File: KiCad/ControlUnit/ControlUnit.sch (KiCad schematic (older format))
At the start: 0 parts

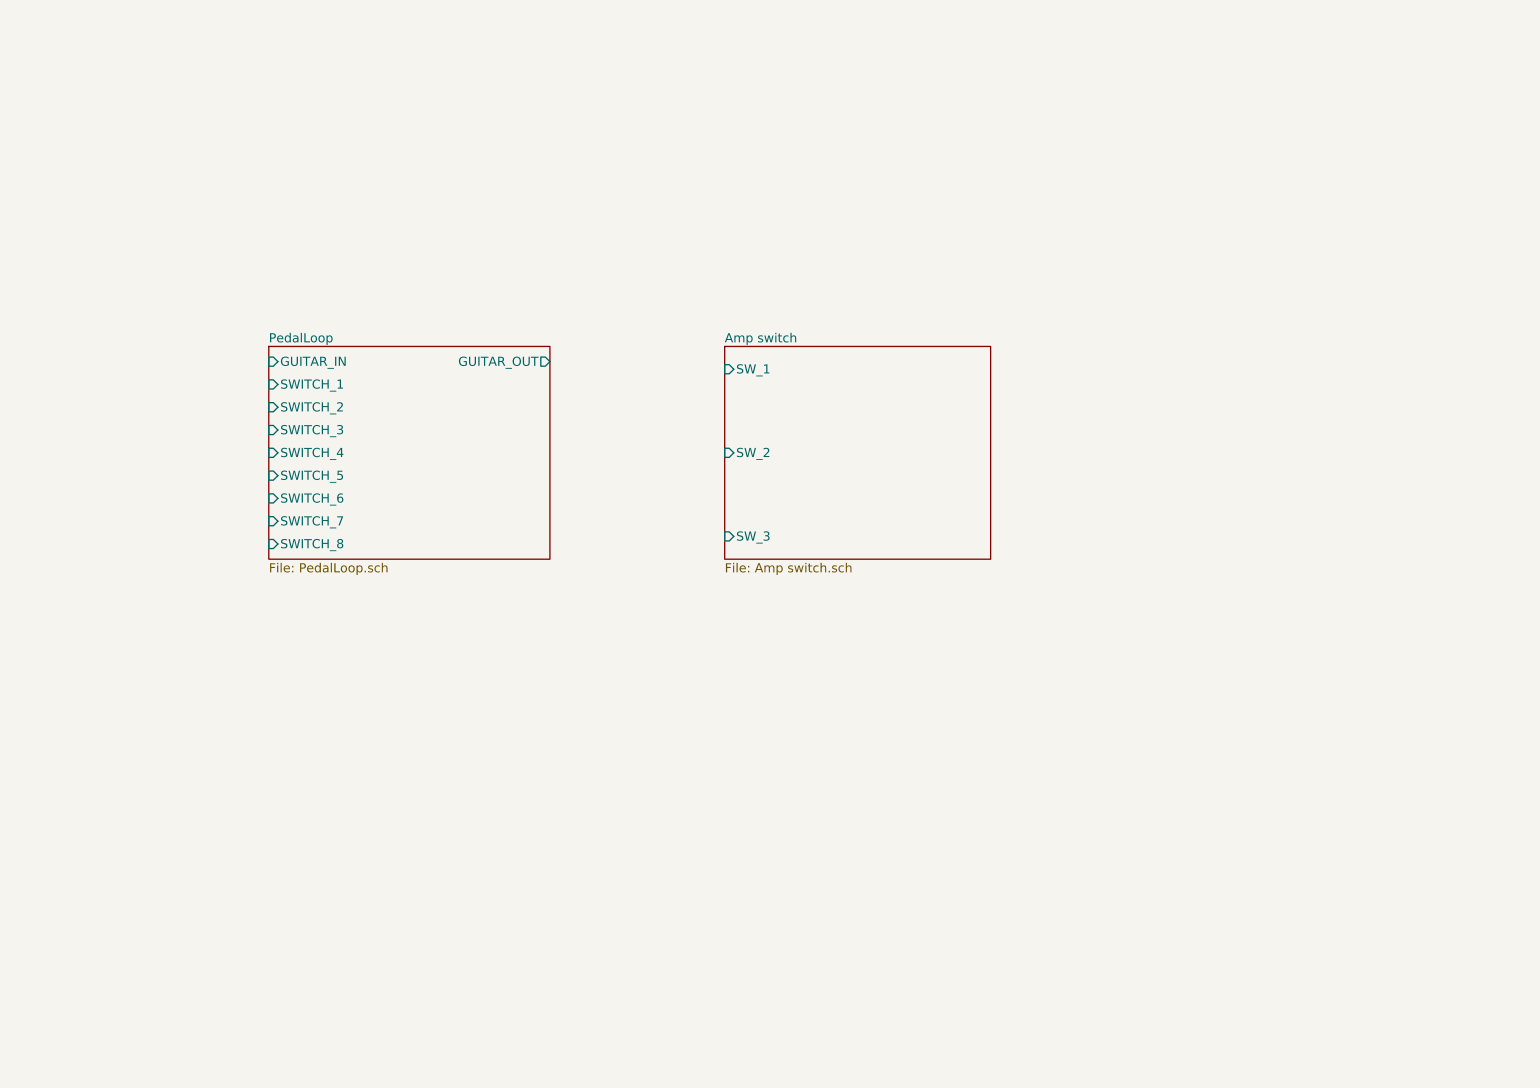
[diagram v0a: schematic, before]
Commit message: Added software for the prototype and made a netlist with footprints for the control unit board
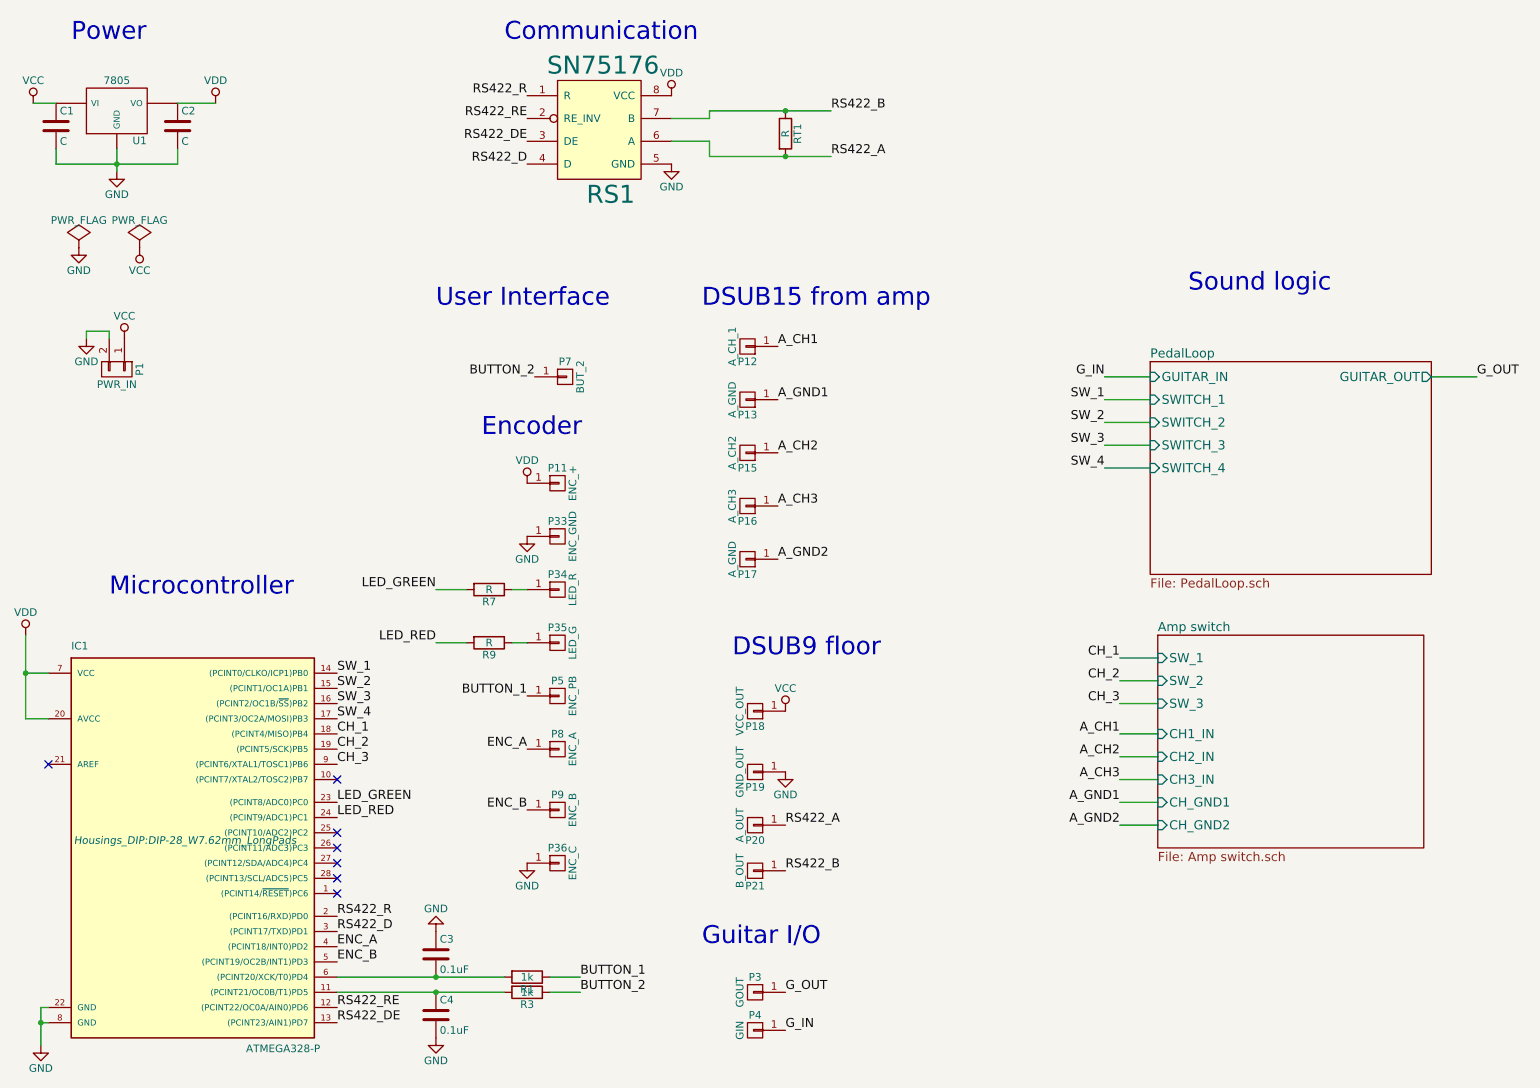
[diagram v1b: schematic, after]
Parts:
- added C1, C2: C, Capacitors_ThroughHole:C_Radial_D8_L13_P3.8, symbol C
- added C3, C4: 0.1uF, Capacitors_ThroughHole:C_Radial_D8_L13_P3.8, symbol C
- added IC1: ATMEGA328-P, Housings_DIP:DIP-28_W7.62mm_LongPads, symbol ATMEGA328-P
- added P1: PWR_IN, Socket_Strips:Socket_Strip_Straight_1x02, symbol CONN_01X02
- added P11: ENC_+, Pin_Headers:Pin_Header_Straight_1x01, symbol CONN_01X01
- added P12: A_CH_1, Pin_Headers:Pin_Header_Straight_1x01, symbol CONN_01X01
- added P13, P17: A_GND, Pin_Headers:Pin_Header_Straight_1x01, symbol CONN_01X01
- added P15: A_CH2, Pin_Headers:Pin_Header_Straight_1x01, symbol CONN_01X01
- added P16: A_CH3, Pin_Headers:Pin_Header_Straight_1x01, symbol CONN_01X01
- added P18: VCC_OUT, Pin_Headers:Pin_Header_Straight_1x01, symbol CONN_01X01
- added P19: GND_OUT, Pin_Headers:Pin_Header_Straight_1x01, symbol CONN_01X01
- added P20: A_OUT, Pin_Headers:Pin_Header_Straight_1x01, symbol CONN_01X01
- added P21: B_OUT, Pin_Headers:Pin_Header_Straight_1x01, symbol CONN_01X01
- added P3: GOUT, Pin_Headers:Pin_Header_Straight_1x01, symbol CONN_01X01
- added P33: ENC_GND, Pin_Headers:Pin_Header_Straight_1x01, symbol CONN_01X01
- added P34: LED_R, Pin_Headers:Pin_Header_Straight_1x01, symbol CONN_01X01
- added P35: LED_G, Pin_Headers:Pin_Header_Straight_1x01, symbol CONN_01X01
- added P36: ENC_C, Pin_Headers:Pin_Header_Straight_1x01, symbol CONN_01X01
- added P4: GIN, Pin_Headers:Pin_Header_Straight_1x01, symbol CONN_01X01
- added P5: ENC_PB, Pin_Headers:Pin_Header_Straight_1x01, symbol CONN_01X01
- added P7: BUT_2, Pin_Headers:Pin_Header_Straight_1x01, symbol CONN_01X01
- added P8: ENC_A, Pin_Headers:Pin_Header_Straight_1x01, symbol CONN_01X01
- added P9: ENC_B, Pin_Headers:Pin_Header_Straight_1x01, symbol CONN_01X01
- added R1, R3: 1k, Resistors_ThroughHole:Resistor_Vertical_RM5mm, symbol R
- added R7, R9, RT1: R, Resistors_ThroughHole:Resistor_Vertical_RM5mm, symbol R
- added RS1: SN75176, Housings_DIP:DIP-8_W7.62mm_LongPads, symbol SN75176
- added U1: 7805, TO_SOT_Packages_THT:SOT126_SOT32_Housing_Vertical_BigPads, symbol 7805
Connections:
- new net: C4.1, IC1.11 ((PCINT21/OC0B/T1)PD5), R3.2
- new net: C3.2, IC1.6 ((PCINT20/XCK/T0)PD4), R1.2
- new net: P35.1 (P1), R9.1
- new net: P34.1 (P1), R7.1
- new net A_CH1: P12.1 (P1)
- new net A_CH2: P15.1 (P1)
- new net A_CH3: P16.1 (P1)
- new net A_GND1: P13.1 (P1)
- new net A_GND2: P17.1 (P1)
- new net BUTTON_1: P5.1 (P1), R1.1
- new net BUTTON_2: P7.1 (P1), R3.1
- new net CH_1: IC1.18 ((PCINT4/MISO)PB4)
- new net CH_2: IC1.19 ((PCINT5/SCK)PB5)
- new net CH_3: IC1.9 ((PCINT6/XTAL1/TOSC1)PB6)
- new net ENC_A: IC1.4 ((PCINT18/INT0)PD2), P8.1 (P1)
- new net ENC_B: IC1.5 ((PCINT19/OC2B/INT1)PD3), P9.1 (P1)
- new net GND: C1.2, C2.2, C3.1, C4.2, IC1.22 (GND), IC1.8 (GND), P1.2 (P2), P19.1 (P1), P33.1 (P1), P36.1 (P1), RS1.5 (GND), U1.GND
- new net G_IN: P4.1 (P1)
- new net G_OUT: P3.1 (P1)
- new net LED_GREEN: IC1.23 ((PCINT8/ADC0)PC0), R7.2
- new net LED_RED: IC1.24 ((PCINT9/ADC1)PC1), R9.2
- new net RS422_A: P20.1 (P1), RS1.6 (A), RT1.2
- new net RS422_B: P21.1 (P1), RS1.7 (B), RT1.1
- new net RS422_D: IC1.3 ((PCINT17/TXD)PD1), RS1.4 (D)
- new net RS422_DE: IC1.13 ((PCINT23/AIN1)PD7), RS1.3 (DE)
- new net RS422_R: IC1.2 ((PCINT16/RXD)PD0), RS1.1 (R)
- new net RS422_RE: IC1.12 ((PCINT22/OC0A/AIN0)PD6), RS1.2 (RE_INV)
- new net SW_1: IC1.14 ((PCINT0/CLKO/ICP1)PB0)
- new net SW_2: IC1.15 ((PCINT1/OC1A)PB1)
- new net SW_3: IC1.16 ((PCINT2/OC1B/~SS~)PB2)
- new net SW_4: IC1.17 ((PCINT3/OC2A/MOSI)PB3)
- new net VCC: C1.1, P1.1 (P1), P18.1 (P1), U1.VI
- new net VDD: C2.1, IC1.20 (AVCC), IC1.7 (VCC), P11.1 (P1), RS1.8 (VCC), U1.VO
- no-connect marks 0 -> 7
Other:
- note added: "Communication"
- note added: "DSUB15 from amp"
- note added: "DSUB9 floor"
- note added: "Encoder"
- note added: "Guitar I/O"
- note added: "Microcontroller"
- note added: "Power"
- note added: "Sound logic"
- note added: "User Interface"

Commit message: Fine tuned PCB design and added multicontact connectors instead of  single connectors
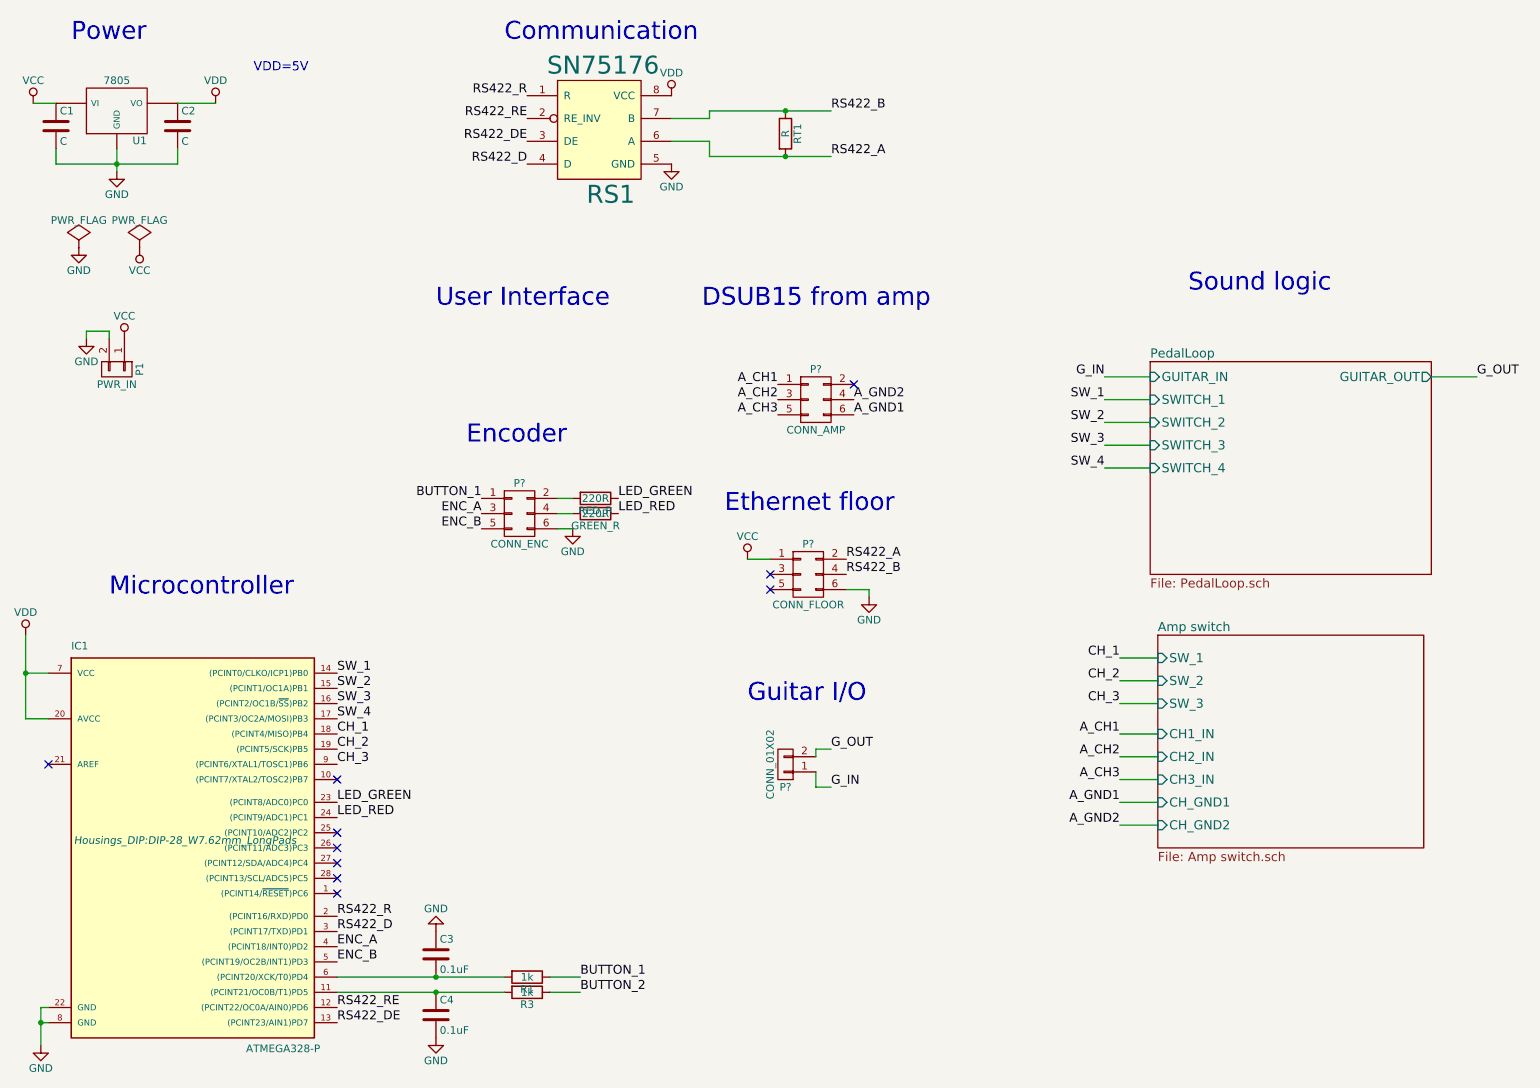
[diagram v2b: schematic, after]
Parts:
- removed P11: ENC_+, Pin_Headers:Pin_Header_Straight_1x01, symbol CONN_01X01
- removed P12: A_CH_1, Pin_Headers:Pin_Header_Straight_1x01, symbol CONN_01X01
- removed P13, P17: A_GND, Pin_Headers:Pin_Header_Straight_1x01, symbol CONN_01X01
- removed P15: A_CH2, Pin_Headers:Pin_Header_Straight_1x01, symbol CONN_01X01
- removed P16: A_CH3, Pin_Headers:Pin_Header_Straight_1x01, symbol CONN_01X01
- removed P18: VCC_OUT, Pin_Headers:Pin_Header_Straight_1x01, symbol CONN_01X01
- removed P19: GND_OUT, Pin_Headers:Pin_Header_Straight_1x01, symbol CONN_01X01
- removed P20: A_OUT, Pin_Headers:Pin_Header_Straight_1x01, symbol CONN_01X01
- removed P21: B_OUT, Pin_Headers:Pin_Header_Straight_1x01, symbol CONN_01X01
- removed P3: GOUT, Pin_Headers:Pin_Header_Straight_1x01, symbol CONN_01X01
- removed P33: ENC_GND, Pin_Headers:Pin_Header_Straight_1x01, symbol CONN_01X01
- removed P34: LED_R, Pin_Headers:Pin_Header_Straight_1x01, symbol CONN_01X01
- removed P35: LED_G, Pin_Headers:Pin_Header_Straight_1x01, symbol CONN_01X01
- removed P36: ENC_C, Pin_Headers:Pin_Header_Straight_1x01, symbol CONN_01X01
- removed P4: GIN, Pin_Headers:Pin_Header_Straight_1x01, symbol CONN_01X01
- removed P5: ENC_PB, Pin_Headers:Pin_Header_Straight_1x01, symbol CONN_01X01
- removed P7: BUT_2, Pin_Headers:Pin_Header_Straight_1x01, symbol CONN_01X01
- removed P8: ENC_A, Pin_Headers:Pin_Header_Straight_1x01, symbol CONN_01X01
- removed P9: ENC_B, Pin_Headers:Pin_Header_Straight_1x01, symbol CONN_01X01
- added P?: CONN_ENC, symbol CONN_02X03
- added P?: CONN_FLOOR, symbol CONN_02X03
- added P?: CONN_01X02, symbol CONN_01X02
- added P?: CONN_AMP, symbol CONN_02X03
- GREEN_R: renamed from R7; value R -> 220R
- RED_R: renamed from R9; value R -> 220R
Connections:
- net A_CH1: now also P?.1 (P1)
- net A_CH2: now also P?.3 (P3)
- net A_CH3: now also P?.5 (P5)
- net A_GND1: now also P?.6 (P6)
- net A_GND2: now also P?.4 (P4)
- net BUTTON_1: now also P?.1 (P1)
- net ENC_A: now also P?.3 (P3)
- net ENC_B: now also P?.5 (P5)
- net GND: now also P?.6 (P6), P?.6 (P6)
- net G_IN: now also P?.1 (P1)
- net G_OUT: now also P?.2 (P2)
- net LED_GREEN: now also RED_R.1; no longer GREEN_R.2
- net LED_RED: now also GREEN_R.1; no longer RED_R.2
- net RS422_A: now also P?.2 (P2)
- net RS422_B: now also P?.4 (P4)
- net VCC: now also P?.1 (P1)
- new net: P?.2 (P2), RED_R.2
- new net: GREEN_R.2, P?.4 (P4)
- no-connect marks 7 -> 10
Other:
- note added: "Ethernet floor"
- note added: "VDD=5V"
- note removed: "DSUB9 floor"
- moved on the sheet: GREEN_R, RED_R
